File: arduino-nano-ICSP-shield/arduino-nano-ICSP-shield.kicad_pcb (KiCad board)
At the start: 2 copper layers, 43.2 x 17.8 mm, 14 parts, among them J1 Analog, J2 Digital, J3 AVR-ISP-6

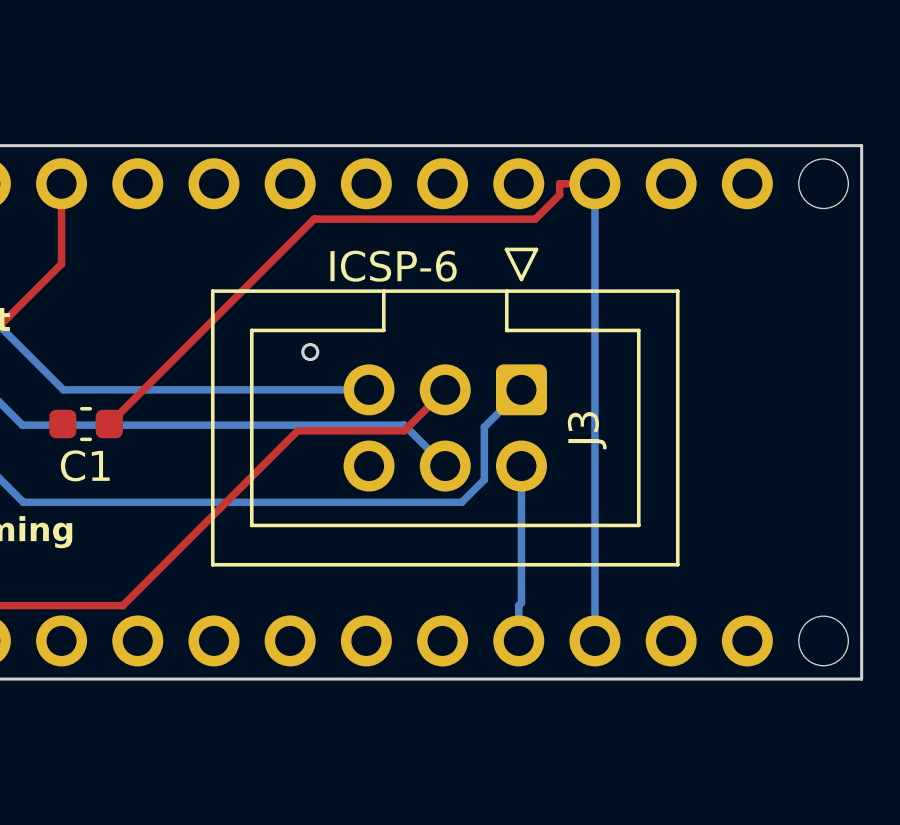
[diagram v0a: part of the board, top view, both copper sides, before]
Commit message: split RESET into RESET & RESET2
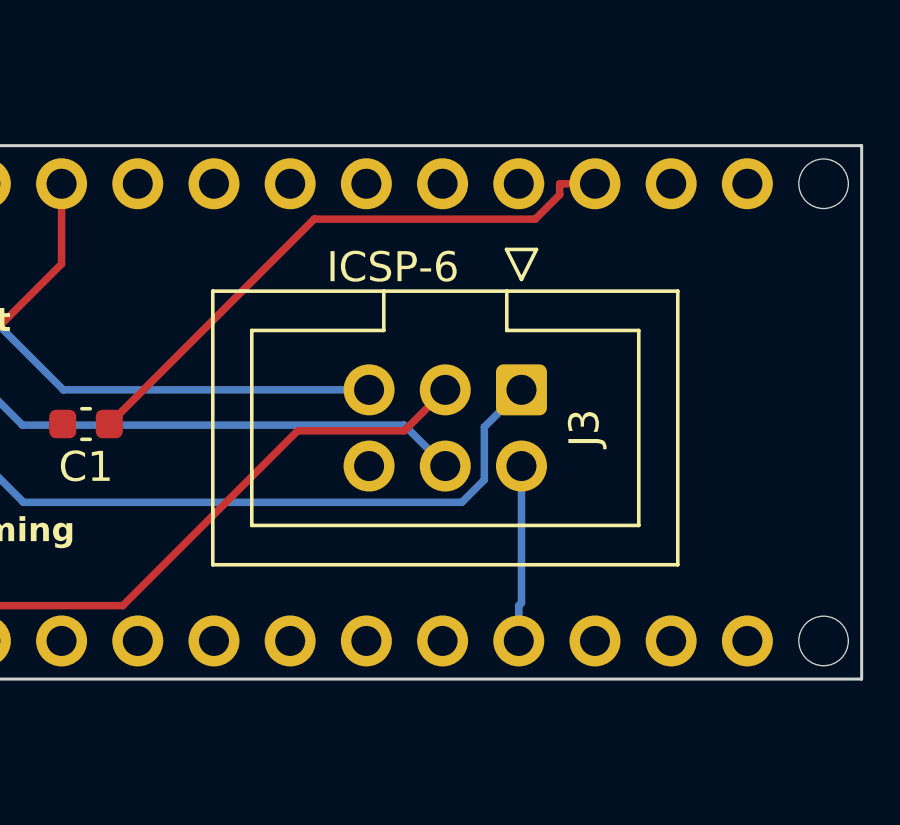
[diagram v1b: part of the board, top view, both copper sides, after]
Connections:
- J1 pad 13: /~{RESET} -> /~{RESET2}
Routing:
- net /~{RESET}: track 35.0 -> 19.7 mm
- net GND: vias 1 -> 0
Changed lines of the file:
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@@
 	(net 30 "Net-(D2-A)")
 	(net 31 "Net-(D3-A)")
+	(net 32 "/~{RESET2}")
 	(footprint "Capacitor_SMD:C_0603_1608Metric"
 		(layer "F.Cu")
@@
 			(layers "*.Cu" "*.Mask")
 			(remove_unused_layers no)
-			(net 2 "/~{RESET}")
+			(net 32 "/~{RESET2}")
 			(pinfunction "Pin_13")
-			(pintype "passive")
+			(pintype "passive+no_connect")
 		)
 		(pad "14" thru_hole oval
@@
 		)
 	)
-	(via
-		(at 124.8 89.1)
-		(size 0.6)
-		(drill 0.4)
-		(layers "F.Cu" "B.Cu")
-		(free yes)
-		(net 1)
-	)
 	(segment
 		(start 134.29 83.49)
@@
 		(net 2)
 	)
-	(segment
-		(start 134.29 83.49)
-		(end 134.29 98.73)
-		(width 0.25)
-		(layer "B.Cu")
-		(net 2)
-	)

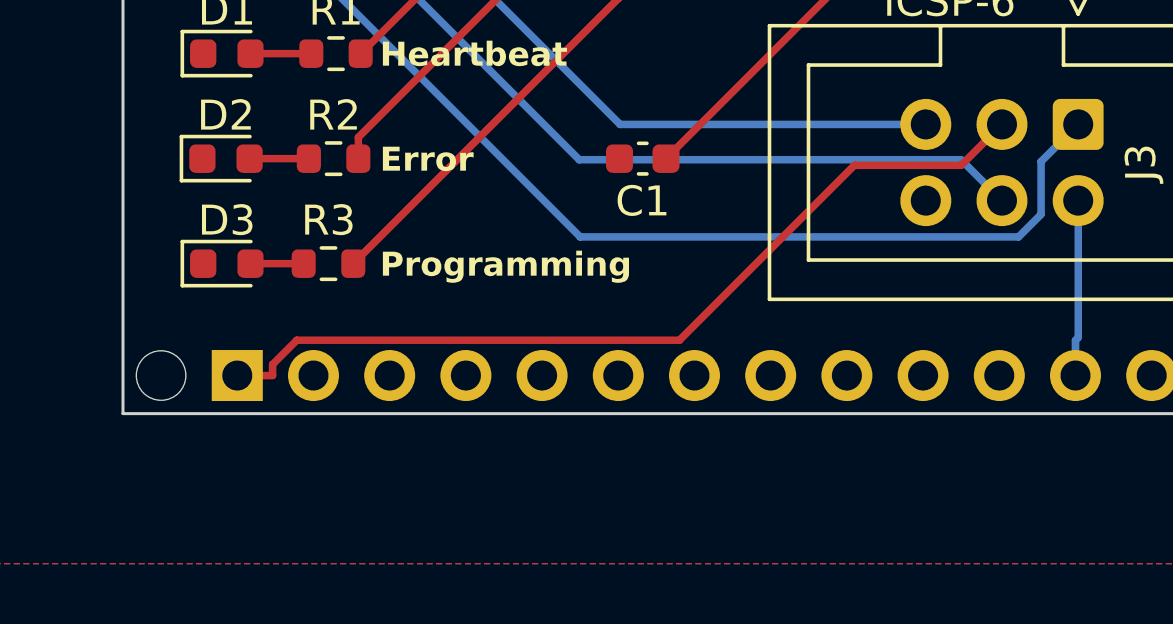
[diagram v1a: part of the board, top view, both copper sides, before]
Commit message: add text
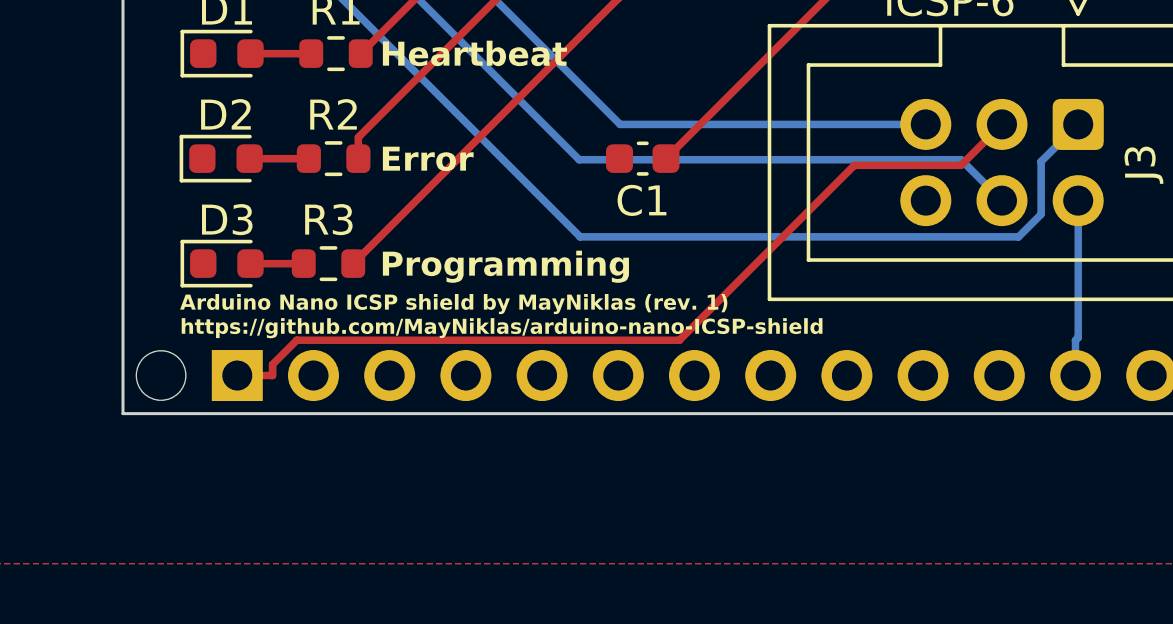
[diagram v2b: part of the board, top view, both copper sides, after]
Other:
- board text added: "${TITLE} by ${COMPANY} (rev. ${REVISION}) ${COMMENT1}"
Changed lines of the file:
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@@
 	(paper "A4")
 	(title_block
+		(title "Arduino Nano ICSP shield")
 		(date "sam. 04 avril 2015")
+		(rev "1")
+		(company "MayNiklas")
+		(comment 1 "https://github.com/MayNiklas/arduino-nano-ICSP-shield")
 	)
 	(layers
@@
 				(bold yes)
 			)
+			(justify left bottom)
+		)
+	)
+	(gr_text "${TITLE} by ${COMPANY} (rev. ${REVISION})\n${COMMENT1}"
+		(at 101.9 97.4 0)
+		(layer "F.SilkS")
+		(effects
+			(font
+				(size 0.5 0.5)
+				(thickness 0.1)
+				(bold yes)
+			)
